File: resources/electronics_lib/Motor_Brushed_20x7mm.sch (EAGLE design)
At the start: 1 part

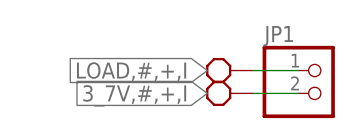
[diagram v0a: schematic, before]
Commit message: Modified motor schematic to make LOAD not busable, added sample verification YAML file.
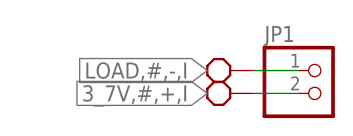
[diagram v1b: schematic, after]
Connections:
- net LOAD,#,+,I renamed LOAD,#,-,I
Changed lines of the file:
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@@
 </segment>
 </net>
-<net name="LOAD,#,+,I" class="0">
+<net name="LOAD,#,-,I" class="0">
 <segment>
 <pinref part="JP1" gate="G$1" pin="1"/>
